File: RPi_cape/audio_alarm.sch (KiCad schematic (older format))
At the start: 81 parts, among them J13 Conn_01x02, J14 Conn_01x02, Q11 MMBT3904, Q12 MMBT3906, Q13 MMBT3904, Q2 MMBT3904, Q5 MMBT3904, Q6 MMBT3904, Q7 DNP, Q8 MMBT3904, U24 TL431A, U25 LM2903, U26 MIC1557, U27 MIC1557, U28 LM4871M

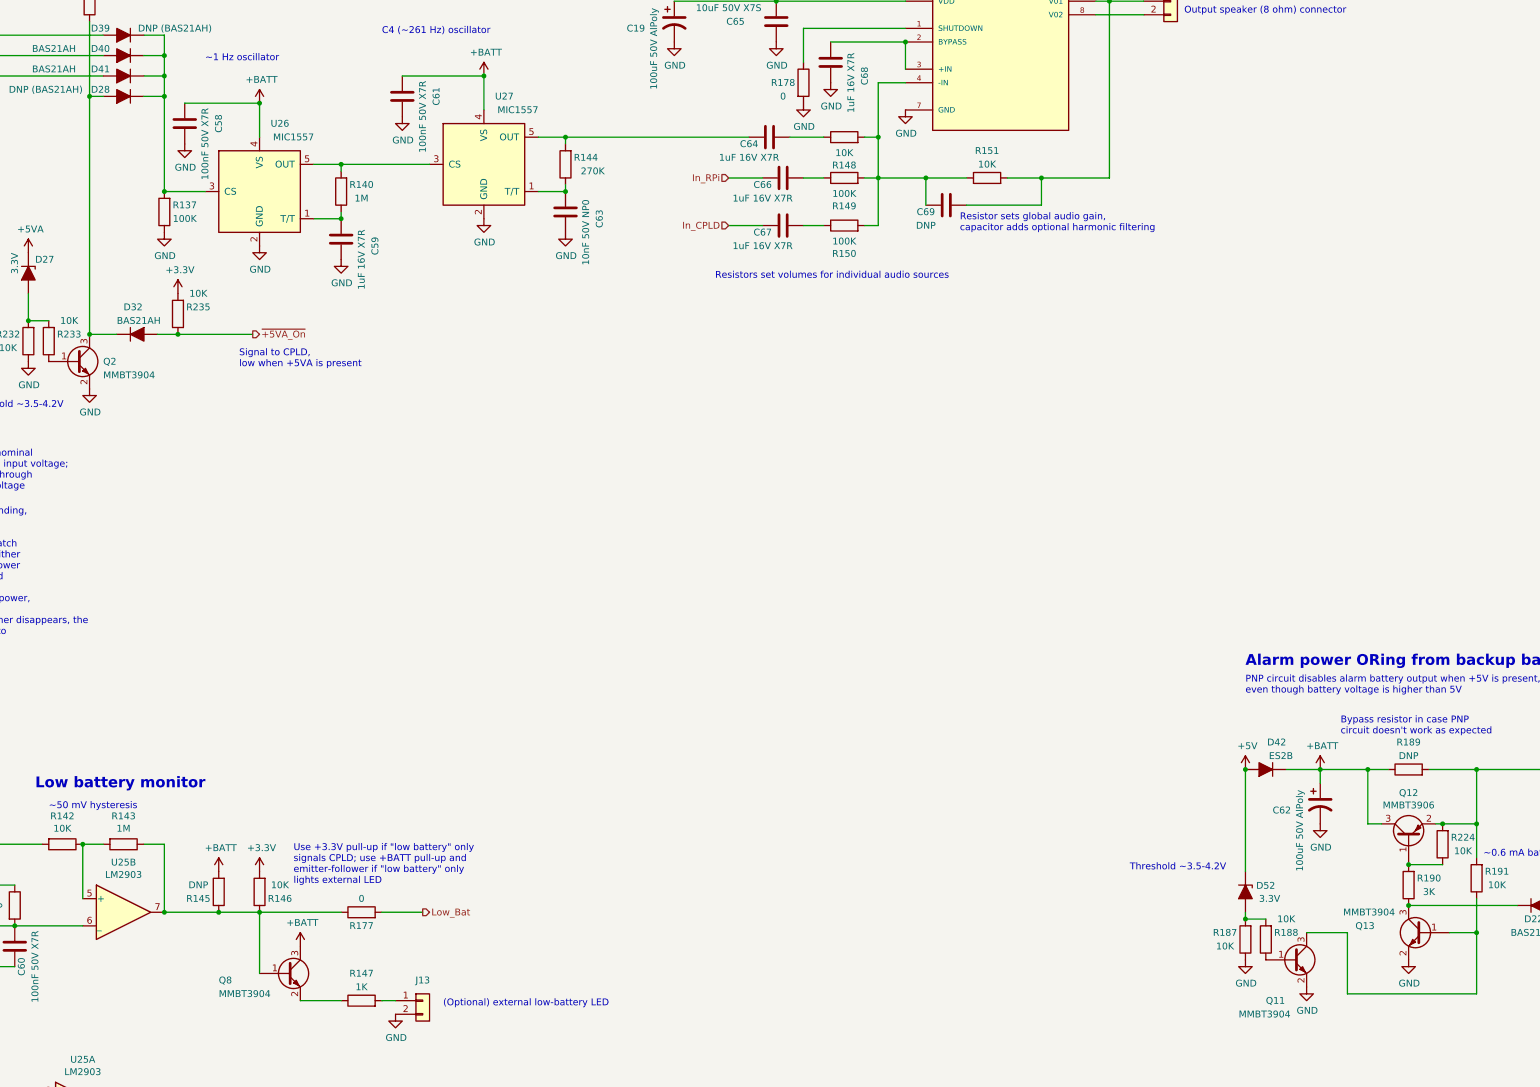
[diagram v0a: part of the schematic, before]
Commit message: Analog upgrades and extra encoder connectors
Renamed a few files
Removed "costing BOM" as difficult to keep up to date, easy to regenerate
Toughened under-voltage detect circuits by adding hysteresis to +5V detect for +BATT diode-OR (R236), filtering to power-down alarm detect input (C85)
Added connector options (J15, J21) for Grayhill C14-series rotary encoder with cable
Changed R190 from 3K to 2.4K to increase overhead on base current required for saturation, and consolidate BOM
Added 3 solderable testpoints for expanding CPLD pin options (TP44-46), adjusted some CPLD pin assignments to allow physical routing to pins
Fixed valve motion detector by changing comparator's hysteresis to AC-only, changing NPN's series resistor to 1K (allows low-enough DC level to count as logic low), and adding optional filtering cap C115 to offset divider
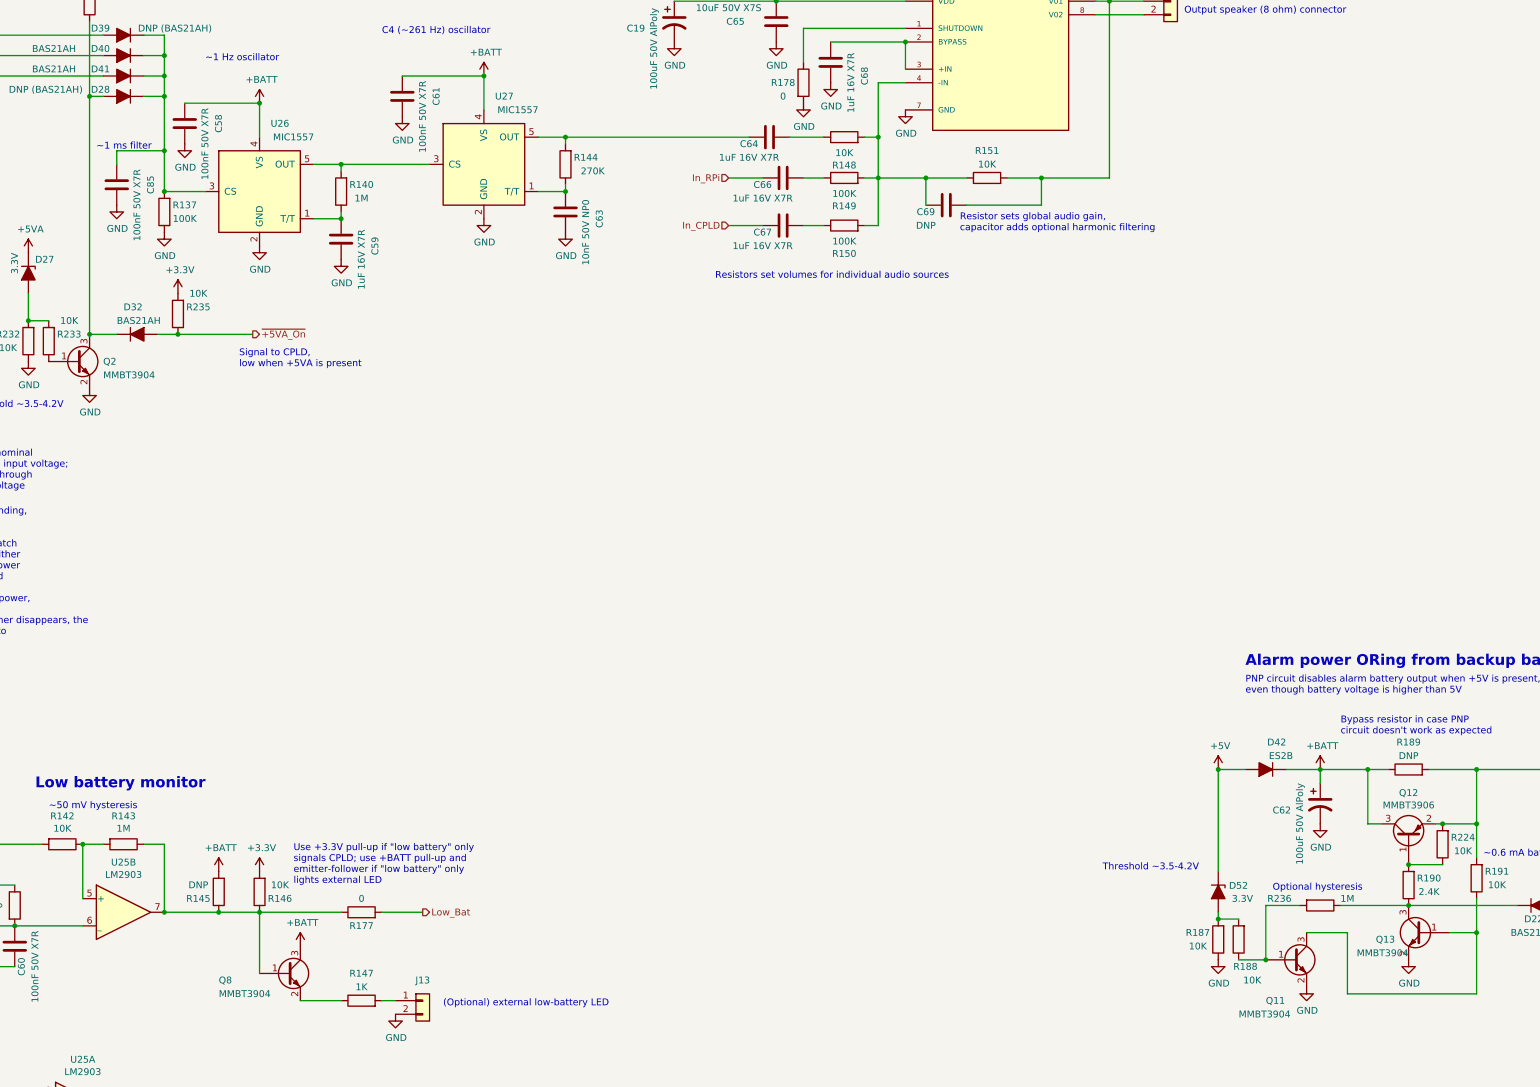
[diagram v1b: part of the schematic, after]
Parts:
- added C85: 100nF 50V X7R, Capacitor_SMD:C_0603_1608Metric, symbol Device:C
- added R236: 1M, Resistor_SMD:R_1206_3216Metric, symbol Device:R
- R190: value 3K -> 2.4K; Part Number RK73H2BTTD3001F -> RK73H2BTTD2401F
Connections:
- net GND: now also C85.1
- net at Q11.1 (B), R188.1: now also R236.2
- net at D22.1 (K), Q13.3 (C), R190.1: now also R236.1
- net at D28.1 (K), D39.1 (K), D40.1 (K)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: now also C85.2
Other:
- note added: "Optional hysteresis"
- note added: "~~1 ms filter"
- moved on the sheet: D52, R187, R188
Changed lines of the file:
@@
 encoding utf-8
 Sheet 9 15
-Title "Audible Alarm"
+Title "Raspberry Pi Hat for JamVent Adaptation"
 Date ""
-Rev "1.7"
+Rev "1.8"
 Comp "US JamVent Team"
 Comment1 "Don Straney"
@@
 L power:+5V #PWR0227
 U 1 1 5F150046
-P 12100 7000
-F 0 "#PWR0227" H 12100 6850 50  0001 C CNN
-F 1 "+5V" H 12115 7173 50  0000 C CNN
-F 2 "" H 12100 7000 50  0001 C CNN
-F 3 "" H 12100 7000 50  0001 C CNN
-	1    12100 7000
+P 11900 7000
+F 0 "#PWR0227" H 11900 6850 50  0001 C CNN
+F 1 "+5V" H 11915 7173 50  0000 C CNN
+F 2 "" H 11900 7000 50  0001 C CNN
+F 3 "" H 11900 7000 50  0001 C CNN
+	1    11900 7000
 	1    0    0    -1
 $EndComp
@@
 AR Path="/5E8E1F08/5F15AD75" Ref="C62"  Part="1"
 F 0 "C62" H 12300 7200 50  0000 L CNN
-F 1 "100uF 50V AlPoly" V 12500 6750 50  0000 L CNN
+F 1 "100uF 50V AlPoly" V 12500 6800 50  0000 L CNN
 F 2 "Capacitor_SMD:CP_Elec_10x10.5" H 12650 7250 50  0001 C CNN
 F 3 "~" H 12650 7250 50  0001 C CNN
@@
 L Device:D_Zener_ALT D?
 U 1 1 5E992FFC
-P 12100 7900
+P 11900 7900
 AR Path="/5E992FFC" Ref="D?"  Part="1"
 AR Path="/5E8AFE9D/5E992FFC" Ref="D?"  Part="1"
 AR Path="/5E8A4ABF/5E992FFC" Ref="D?"  Part="1"
 AR Path="/5E8E1F08/5E992FFC" Ref="D52"  Part="1"
-F 0 "D52" V 12054 7979 50  0000 L CNN
-F 1 "3.3V" V 12150 8000 50  0000 L CNN
-F 2 "Ventilator:D_SOD-123" H 12100 7900 50  0001 C CNN
-F 3 "~" H 12100 7900 50  0001 C CNN
-F 4 "ON Semiconductor" H 12100 7900 50  0001 C CNN "Manufacturer"
-F 5 "MMSZ4684T1G" H 12100 7900 50  0001 C CNN "Part Number"
-	1    12100 7900
+F 0 "D52" V 11854 7979 50  0000 L CNN
+F 1 "3.3V" V 11950 8000 50  0000 L CNN
+F 2 "Ventilator:D_SOD-123" H 11900 7900 50  0001 C CNN
+F 3 "~" H 11900 7900 50  0001 C CNN
+F 4 "ON Semiconductor" H 11900 7900 50  0001 C CNN "Manufacturer"
+F 5 "MMSZ4684T1G" H 11900 7900 50  0001 C CNN "Part Number"
+	1    11900 7900
 	0    1    1    0
 $EndComp
@@
 L Device:R R?
 U 1 1 5E993008
-P 12250 8250
+P 12050 8250
 AR Path="/5E993008" Ref="R?"  Part="1"
 AR Path="/5E8AFE9D/5E993008" Ref="R?"  Part="1"
 AR Path="/5E8C8865/5E993008" Ref="R?"  Part="1"
 AR Path="/5E8E1F08/5E993008" Ref="R188"  Part="1"
-F 0 "R188" H 12100 8200 50  0000 C CNN
-F 1 "10K" H 12100 8100 50  0000 C CNN
-F 2 "Resistor_SMD:R_1206_3216Metric" V 12180 8250 50  0001 C CNN
-F 3 "~" H 12250 8250 50  0001 C CNN
-F 4 "KOA Speer" H 12250 8250 50  0001 C CNN "Manufacturer"
-F 5 "RK73H2BTTD1002F" H 12250 8250 50  0001 C CNN "Part Number"
-	1    12250 8250
-	-1   0    0    1
-$EndComp
-Wire Wire Line
-	12250 8100 12100 8100
-Wire Wire Line
-	12100 8100 12100 8050
+F 0 "R188" H 12000 8450 50  0000 C CNN
+F 1 "10K" H 11950 8550 50  0000 C CNN
+F 2 "Resistor_SMD:R_1206_3216Metric" V 11980 8250 50  0001 C CNN
+F 3 "~" H 12050 8250 50  0001 C CNN
+F 4 "KOA Speer" H 12050 8250 50  0001 C CNN "Manufacturer"
+F 5 "RK73H2BTTD1002F" H 12050 8250 50  0001 C CNN "Part Number"
+	1    12050 8250
+	-1   0    0    1
+$EndComp
+Wire Wire Line
+	12050 8100 11900 8100
+Wire Wire Line
+	11900 8100 11900 8050
 $Comp
 L power:GND #PWR?
@@
 L Device:R R?
 U 1 1 5E993016
-P 12100 8250
+P 11900 8250
 AR Path="/5E993016" Ref="R?"  Part="1"
 AR Path="/5E8AFE9D/5E993016" Ref="R?"  Part="1"
 AR Path="/5E8C8865/5E993016" Ref="R?"  Part="1"
 AR Path="/5E8E1F08/5E993016" Ref="R187"  Part="1"
-F 0 "R187" H 12250 8200 50  0000 C CNN
-F 1 "10K" H 12250 8300 50  0000 C CNN
-F 2 "Resistor_SMD:R_1206_3216Metric" V 12030 8250 50  0001 C CNN
-F 3 "~" H 12100 8250 50  0001 C CNN
-F 4 "KOA Speer" H 12100 8250 50  0001 C CNN "Manufacturer"
-F 5 "RK73H2BTTD1002F" H 12100 8250 50  0001 C CNN "Part Number"
-	1    12100 8250
-	-1   0    0    1
-$EndComp
-Connection ~ 12100 8100
+F 0 "R187" H 12050 8200 50  0000 C CNN
+F 1 "10K" H 12050 8300 50  0000 C CNN
+F 2 "Resistor_SMD:R_1206_3216Metric" V 11830 8250 50  0001 C CNN
+F 3 "~" H 11900 8250 50  0001 C CNN
+F 4 "KOA Speer" H 11900 8250 50  0001 C CNN "Manufacturer"
+F 5 "RK73H2BTTD1002F" H 11900 8250 50  0001 C CNN "Part Number"
+	1    11900 8250
+	-1   0    0    1
+$EndComp
+Connection ~ 11900 8100
 $Comp
 L power:GND #PWR?
 U 1 1 5E99301D
-P 12100 8400
+P 11900 8400
 AR Path="/5E99301D" Ref="#PWR?"  Part="1"
 AR Path="/5E8E1F08/5E99301D" Ref="#PWR0326"  Part="1"
-F 0 "#PWR0326" H 12100 8150 50  0001 C CNN
-F 1 "GND" H 12105 8227 50  0000 C CNN
-F 2 "" H 12100 8400 50  0001 C CNN
-F 3 "" H 12100 8400 50  0001 C CNN
-	1    12100 8400
-	1    0    0    -1
-$EndComp
-Wire Wire Line
-	12100 7000 12100 7750
-Connection ~ 12100 7000
+F 0 "#PWR0326" H 11900 8150 50  0001 C CNN
+F 1 "GND" H 11905 8227 50  0000 C CNN
+F 2 "" H 11900 8400 50  0001 C CNN
+F 3 "" H 11900 8400 50  0001 C CNN
+	1    11900 8400
+	1    0    0    -1
+$EndComp
+Wire Wire Line
+	11900 7000 11900 7750
 $Comp
 L Transistor_BJT:MMBT3906 Q12
@@
 U 1 1 5E9AF013
 P 13400 8200
-F 0 "Q13" H 13750 8250 50  0000 L CNN
-F 1 "MMBT3904" H 13600 8350 50  0000 L CNN
+F 0 "Q13" H 13600 8150 50  0000 L CNN
+F 1 "MMBT3904" H 13500 8050 50  0000 L CNN
 F 2 "Ventilator:SOT-23" H 13600 8125 50  0001 L CIN
 F 3 "https://www.fairchildsemi.com/datasheets/2N/2N3904.pdf" H 13400 8200 50  0001 L CNN
@@
 AR Path="/5E8E1F08/5E9BB72E" Ref="R190"  Part="1"
 F 0 "R190" H 13150 7800 50  0000 C CNN
-F 1 "3K" H 13150 7900 50  0000 C CNN
+F 1 "2.4K" H 13150 7900 50  0000 C CNN
 F 2 "Resistor_SMD:R_1206_3216Metric" V 13230 7850 50  0001 C CNN
 F 3 "~" H 13300 7850 50  0001 C CNN
 F 4 "KOA Speer" H 13300 7850 50  0001 C CNN "Manufacturer"
-F 5 "RK73H2BTTD3001F" H 13300 7850 50  0001 C CNN "Part Number"
+F 5 "RK73H2BTTD2401F" H 13300 7850 50  0001 C CNN "Part Number"
 	1    13300 7850
 	-1   0    0    1
@@
 Text Notes 12100 6450 0    50   ~ 0
 PNP circuit disables alarm battery output when +5V is present,\neven though battery voltage is higher than 5V
-Text Notes 11250 7750 0    50   ~ 0
+Text Notes 11050 7750 0    50   ~ 0
 Threshold ~~3.5-4.2V
 Text Notes 700  6100 0    50   ~ 0
@@
 Connection ~ 4150 2050
 Wire Wire Line
-	4150 2050 4150 2750
+	4150 2050 4150 2450
 Wire Wire Line
 	3700 2050 3600 2050
@@
 Text Notes 4700 4050 0    50   ~ 0
 Signal to CPLD,\nlow when +5VA is present
+$Comp
+L Device:R R?
+U 1 1 5F0C0AAB
+P 12650 8000
+AR Path="/5F0C0AAB" Ref="R?"  Part="1"
+AR Path="/5E8AFE9D/5F0C0AAB" Ref="R?"  Part="1"
+AR Path="/5E8A4ABF/5F0C0AAB" Ref="R?"  Part="1"
+AR Path="/5E8E1F08/5F0C0AAB" Ref="R236"  Part="1"
+F 0 "R236" V 12600 7700 50  0000 C CNN
+F 1 "1M" V 12600 8200 50  0000 C CNN
+F 2 "Resistor_SMD:R_1206_3216Metric" V 12580 8000 50  0001 C CNN
+F 3 "~" H 12650 8000 50  0001 C CNN
+F 4 "KOA Speer" H 12650 8000 50  0001 C CNN "Manufacturer"
+F 5 "RK73H2BTTD1004F" H 12650 8000 50  0001 C CNN "Part Number"
+	1    12650 8000
+	0    1    1    0
+$EndComp
+Wire Wire Line
+	12800 8000 13300 8000
+Wire Wire Line
+	12250 8400 12250 8000
+Wire Wire Line
+	12250 8000 12500 8000
+Wire Wire Line
+	11900 7000 12100 7000
+Connection ~ 11900 7000
+Wire Wire Line
+	12050 8400 12250 8400
+Connection ~ 12250 8400
+Text Notes 12300 7900 0    50   ~ 0
+Optional hysteresis
+$Comp
+L Device:C C?
+U 1 1 5F0F65B2
+P 3800 2700
+AR Path="/5F0F65B2" Ref="C?"  Part="1"
+AR Path="/5E8AFE9D/5F0F65B2" Ref="C?"  Part="1"
+AR Path="/5E8FBD97/5F0F65B2" Ref="C?"  Part="1"
+AR Path="/5E8E0754/5F0F65B2" Ref="C?"  Part="1"
+AR Path="/5E8DFCAD/5F0F65B2" Ref="C?"  Part="1"
+AR Path="/5E8DEDC0/5F0F65B2" Ref="C?"  Part="1"
+AR Path="/5E8C8865/5F0F65B2" Ref="C?"  Part="1"
+AR Path="/5E8E1F08/5F0F65B2" Ref="C85"  Part="1"
+F 0 "C85" V 3550 2700 50  0000 C CNN
+F 1 "100nF 50V X7R" V 3650 2850 50  0000 C CNN
+F 2 "Capacitor_SMD:C_0603_1608Metric" H 3838 2550 50  0001 C CNN
+F 3 "~" H 3800 2700 50  0001 C CNN
+F 4 "AVX" H 3800 2700 50  0001 C CNN "Manufacturer"
+F 5 "06035C104JAT2A" H 3800 2700 50  0001 C CNN "Part Number"
+	1    3800 2700
+	-1   0    0    1
+$EndComp
+$Comp
+L power:GND #PWR?
+U 1 1 5F0F65B8
+P 3800 2850
+AR Path="/5F0F65B8" Ref="#PWR?"  Part="1"
+AR Path="/5E8AFE9D/5F0F65B8" Ref="#PWR?"  Part="1"
+AR Path="/5E8FBD97/5F0F65B8" Ref="#PWR?"  Part="1"
+AR Path="/5E8E0754/5F0F65B8" Ref="#PWR?"  Part="1"
+AR Path="/5E8DFCAD/5F0F65B8" Ref="#PWR?"  Part="1"
+AR Path="/5E8DEDC0/5F0F65B8" Ref="#PWR?"  Part="1"
+AR Path="/5E8C8865/5F0F65B8" Ref="#PWR?"  Part="1"
+AR Path="/5E8E1F08/5F0F65B8" Ref="#PWR0379"  Part="1"
+F 0 "#PWR0379" H 3800 2600 50  0001 C CNN
+F 1 "GND" H 3805 2677 50  0000 C CNN
+F 2 "" H 3800 2850 50  0001 C CNN
+F 3 "" H 3800 2850 50  0001 C CNN
+	1    3800 2850
+	1    0    0    -1
+$EndComp
+Wire Wire Line
+	3800 2550 3800 2450
+Wire Wire Line
+	3800 2450 4150 2450
+Connection ~ 4150 2450
+Wire Wire Line
+	4150 2450 4150 2750
+Text Notes 3650 2450 0    50   ~ 0
+~~1 ms filter
 $EndSCHEMATC
